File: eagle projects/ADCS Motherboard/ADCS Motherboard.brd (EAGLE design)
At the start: 91 x 91 mm, 127 parts, among them J1 HDR_10_EZFET_DEBUGGER, J3 HDR_2X5_GRPB052VWQS-RC, Q1 PMV16XN, Q2 IRLML6246TRPBF, Q3 IRLML2246TRPBF, U1 MSP430F5529IPN, U2 LMV321, U3 ADS7841E_2K5, U4 LMV321, U5 LMV321, U7 HMC1053, Y1 32.768kHz, Y2 CSTCR4M00G15L99, Y3 32.768kHz

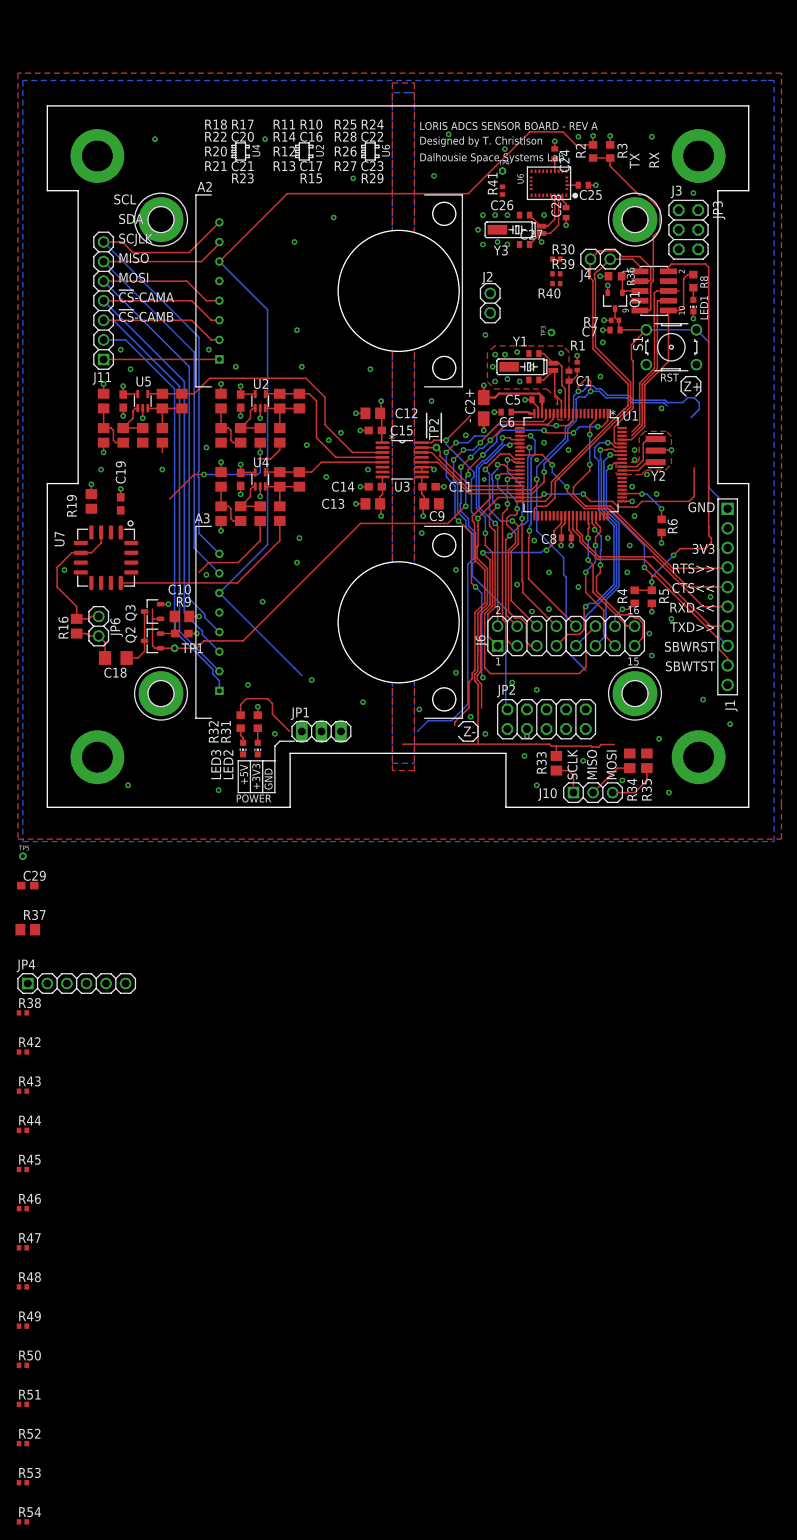
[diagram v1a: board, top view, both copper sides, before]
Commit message: Major layout changes check point
New connectors, analog plane reshape, moved msp430
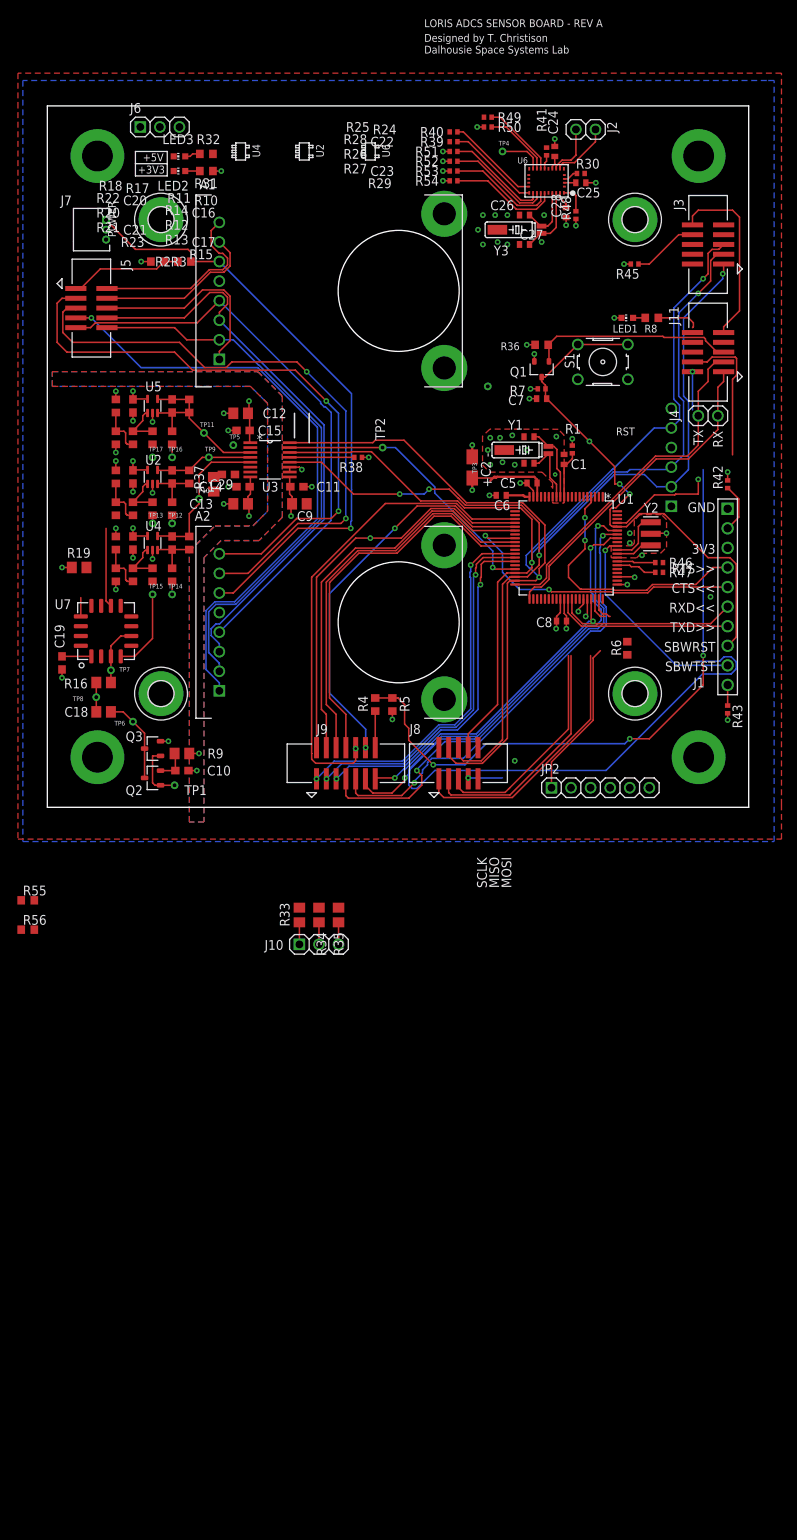
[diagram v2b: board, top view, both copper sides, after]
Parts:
- removed A3: ARDUCAM_OV5642, my_library:ARDUCAM
- removed JP1: (no value), pinhead:1X03
- removed JP3: (no value), pinhead:2X03
- removed JP6: (no value), my_library:1X02
- removed R44: 5.1M, rcl:R0402
- added A1: ARDUCAM_OV5642, my_library:ARDUCAM
- added J5, J8: CNC_3221-10-0300-00, my_library:CNC_3221-10-0300-00
- added J7: TE-1734829-3, my_library:TE-1734829-3
- added J9: CNC_3221-14-0300-00, my_library:CNC_3221-14-0300-00
- added R55, R56: 5.1M, rcl:R0603
- added TP10, TP11, TP12, TP13, TP14, TP15, TP16, TP17, TP6, TP7, TP8, TP9: TESTPOINT, my_library:TP_P76H50
- C17, C21, C23: device rcl:C0805 -> rcl:C0603
- C18: device resistor:C1206 -> rcl:C0805
- J11: value (none) -> CNC_3221-10-0300-00; device my_library:1X07 -> my_library:CNC_3221-10-0300-00
- J3: value HDR_2X5_GRPB052VWQS-RC -> CNC_3221-10-0300-00; device my_library:GRPB052VWQS-RC -> my_library:CNC_3221-10-0300-00
- J6: device my_library:2X08 -> my_library:1X03
- JP2: device pinhead:2X05 -> my_library:1X06
- R10, R11, R12, R13, R14, R15, R17, R18, R20, R21, R22, R23, R24, R25, R26, R27, R28, R29: device rcl:R0805 -> rcl:R0603
- R16: value 0R -> 1R
- moved R54 182.7 mm to (52.7, 81.3)
- moved R53 179.1 mm to (52.7, 82.5)
- moved R52 175.5 mm to (52.7, 83.8)
- moved R51 171.9 mm to (52.7, 85.1)
- moved R50 171.6 mm to (57.1, 88.3)
- moved R49 168.0 mm to (57.1, 89.5)
- moved R48 156.5 mm to (68.6, 76.8), turned to 90 degrees
- moved R45 141.8 mm to (76.2, 70.5), turned to 180 degrees
- moved R47 120.4 mm to (79.4, 30.5)
- moved R46 117.6 mm to (79.4, 31.8)
- moved R42 117.4 mm to (88.3, 41.9), turned to 90 degrees
- moved R43 104.0 mm to (88.3, 12.7), turned to 270 degrees
- moved JP4 103.0 mm to (81.0, 45.4), flipped to the bottom, turned to 90 degrees
- moved J6 84.5 mm to (14.6, 88.3)
- moved R38 84.2 mm to (40.3, 45.4), turned to 180 degrees
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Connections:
- removed net !CS!_CAM_A: A2.1, J11.1
- removed net !CS!_CAM_B: A3.1, J11.2
- removed net N$18: JP2.8, R45.1
- removed net N$19: JP2.10, R44.1
- removed net PAYLOAD_MISO: A2.3, A3.3, J11.4
- removed net PAYLOAD_MOSI: A2.2, A3.2, J11.3
- removed net PAYLOAD_SCL: A2.8, A3.8, J11.7
- removed net PAYLOAD_SCLK: A2.4, A3.4, J11.5
- removed net PAYLOAD_SDA: A2.7, A3.7, J11.6
- removed net SEN_BRD_5V_PRESENT: J3.9, R2.1, R3.2
- new net CAMERA-1_CS: A1.1, J5.6
- new net CAMERA-1_SCL: A1.8, J5.2
- new net CAMERA-1_SDA: A1.7, J5.4
- new net CAMERA-2_CS: A2.1, J5.7
- new net CAMERA-2_SCL: A2.8, J5.3
- new net CAMERA-2_SDA: A2.7, J5.5
- new net CAMERA_MISO: A1.3, A2.3, J5.8
- new net CAMERA_MOSI: A1.2, A2.2, J5.10
- new net CAMERA_SCLK: A1.4, A2.4, J5.9
- new net CAM_5V_PRESENT: J5.1, R2.1, R3.2
- new net N$55: J8.9, R56.2
- new net N$57: J8.10, R55.1
- new net N$58: J3.8, R45.1
- new net P1.0: JP2.6, U1.21
- new net P1.1: JP2.5, U1.22
- new net TB0.3: JP2.2, U1.58
- new net TB0.4: JP2.1, U1.59
- new net TB0.5: JP2.4, U1.42
- new net TB0.6: JP2.3, U1.43
- new net Z-_SUN_3V_PRESENT: J11.9, J3.10
- net !CS!_CURRENT_SENSE_1: now also J8.3; no longer JP3.1
- net !CS!_CURRENT_SENSE_2: now also J8.5; no longer JP3.3
- net !CS!_SUN_X+: now also J3.2; no longer JP2.2
- net !CS!_SUN_X-: now also J3.7; no longer JP2.7
- net !CS!_SUN_Y+: now also J3.4; no longer JP2.4
- net !CS!_SUN_Y-: now also J3.9; no longer JP2.9
- net !CS!_SUN_Z+: now also JP4.4; no longer JP4.5
- net !CS!_SUN_Z-: now also J3.6; no longer JP2.6
- net +3V3: now also J11.7, J6.2, J7.2; no longer J3.7, JP1.2
- net +5V: now also A1.6, J6.1, J7.1; no longer A3.6, JP1.1
- net ACT_BRD_3V_PRESENT: now also J11.4, J8.7; no longer J3.4, JP3.5
- net ACT_BRD_5V_PRESENT: now also J9.14; no longer J6.14
- net ACT_BRD_5V_SHIFTED: now also J11.2; no longer J3.2
- net B_MEAS_X: now also TP10.1
- net B_MEAS_Y: now also TP9.1
- net B_MEAS_Z: now also TP11.1
- net GND: now also A1.5, A1.P$1, A1.P$2, A2.P$1, A2.P$2, J6.3, J7.3, R55.2, R56.1; no longer A3.5, JP1.3, R44.2
- net MAG_X_FIN: now also J9.10; no longer J6.10
- net MAG_X_RIN: now also J9.12; no longer J6.12
- net MAG_Y_FIN: now also J9.6; no longer J6.6
- net MAG_Y_RIN: now also J9.8; no longer J6.8
- net MAG_Z_FIN: now also J9.2; no longer J6.2
- net MAG_Z_RIN: now also J9.4; no longer J6.4
- net MSP430_ACTIVE: now also J11.10; no longer J3.10
- net MSP_OBC_RESET: now also J11.5; no longer J3.5
- net N$35: now also TP8.1; no longer JP6.2
- net N$37: now also TP7.1; no longer JP6.1
- net N$9: now also TP6.1
- net OUT_A_N: now also TP13.1
- net OUT_A_P: now also TP12.1
- net OUT_B_N: now also TP15.1
- net OUT_B_P: now also TP14.1
- net OUT_C_N: now also TP17.1
- net OUT_C_P: now also TP16.1
- net RESERVED_1: now also J11.6; no longer J3.6
- net RESERVED_2: now also J11.8; no longer J3.8
- net RW_X_DIR: now also J9.7; no longer J6.7
- net RW_X_OUTFG: now also J9.13; no longer J6.13
- net RW_X_SPEED_CTRL: now also J9.1; no longer J6.1
- net RW_Y_DIR: now also J9.9; no longer J6.9
- net RW_Y_OUTFG: now also J8.1; no longer J6.15
- net RW_Y_SPEED_CTRL: now also J9.3; no longer J6.3
- net RW_Z_DIR: now also J9.11; no longer J6.11
- net RW_Z_OUTFG: now also J8.2; no longer J6.16
- net RW_Z_SPEED_CTRL: now also J9.5; no longer J6.5
- net UCA0RXD: now also J11.1; no longer J3.1
- net UCA0TXD: now also J11.3; no longer J3.3
- net UCB0_SPI_CLK: now also J3.5, J8.4, JP4.5; no longer JP2.5, JP3.2, JP4.4
- net UCB0_SPI_MISO: now also J3.1, J8.6; no longer JP2.1, JP3.4
- net UCB0_SPI_MOSI: now also J3.3, J8.8; no longer JP2.3, JP3.6
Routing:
- net RW_Z_DIR: track 28.8 -> 124.0 mm, vias 1 -> 2
- net CAMERA-2_CS: track 0.00 -> 79.6 mm, vias 0 -> 1
- net CAMERA-2_SCL: track 0.00 -> 78.6 mm, vias 0 -> 2
- net CAMERA-2_SDA: track 0.00 -> 78.5 mm, vias 0 -> 2
- net CAMERA_MISO: track 0.00 -> 76.1 mm
- net CAMERA_SCLK: track 0.00 -> 75.2 mm
- net HMC1053_RESET: track 81.5 -> 7.52 mm, vias 6 -> 0
- net CAMERA_MOSI: track 0.00 -> 72.9 mm
- net PAYLOAD_MOSI: track 68.6 -> 0.00 mm
- net PAYLOAD_MISO: track 67.8 -> 0.00 mm
- net PAYLOAD_SCLK: track 67.8 -> 0.00 mm
- net PAYLOAD_SCL: track 64.0 -> 0.00 mm
- net PAYLOAD_SDA: track 62.9 -> 0.00 mm
- net !CS!_SUN_Z-: track 55.9 -> 0.00 mm, vias 3 -> 0
- net !CS!_CAM_B: track 53.4 -> 0.00 mm
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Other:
- outline, holes or cut-outs redrawn
- board text removed: "!CS!-CAMA"
- board text removed: "!CS!-CAMB"
- board text removed: "J3"
- board text removed: "SCJLK"
- board text removed: "SCL"
- board text removed: "SDA"
- board text removed: "Z+"
- board text removed: "Z-"

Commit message: Draft of Rev B done
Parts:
- added TP18, TP19: TESTPOINT, my_library:TP_P76H50
- moved J10 112.0 mm to (74.9, 87.0), turned to 180 degrees
- moved R33 107.0 mm to (77.5, 83.2), turned to 90 degrees
- moved R34 104.9 mm to (74.9, 83.2), turned to 90 degrees
- moved R35 103.1 mm to (72.4, 83.2), turned to 90 degrees
- moved R56 71.2 mm to (63.2, 11.4), turned to 270 degrees
- moved R55 67.7 mm to (61.0, 11.4), turned to 90 degrees
- moved R4 39.7 mm to (82.2, 13.3)
- moved R5 39.7 mm to (84.5, 13.3)
- moved R40 24.8 mm to (60.6, 64.1), turned to 270 degrees
- moved R39 24.1 mm to (61.9, 64.1), turned to 270 degrees
- moved R51 23.6 mm to (63.5, 64.1), turned to 90 degrees
- moved R52 23.1 mm to (64.8, 64.1), turned to 90 degrees
- moved R53 22.7 mm to (66.0, 64.1), turned to 90 degrees
- moved R54 22.5 mm to (67.3, 64.1), turned to 90 degrees
- moved R50 19.4 mm to (57.1, 68.9)
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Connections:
- net P1.0: now also JP2.1; no longer JP2.6
- net P1.1: now also JP2.2; no longer JP2.5
- net TB0.3: now also JP2.5; no longer JP2.2
- net TB0.4: now also JP2.6; no longer JP2.1
- net TB0.5: now also JP2.3; no longer JP2.4
- net TB0.6: now also JP2.4; no longer JP2.3
- net UCB1_I2C_SCL: now also TP18.1
- net UCB1_I2C_SDA: now also TP19.1
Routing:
- net HMC1053_RESET: track 7.52 -> 98.8 mm, vias 0 -> 1
- net !CS!_SUN_X+: track 0.00 -> 79.2 mm, vias 0 -> 2
- net RW_Z_DIR: track 124.0 -> 58.0 mm
- net ACT_BRD_3V_PRESENT: track 23.3 -> 82.6 mm, vias 1 -> 4
- net RESERVED_2: track 0.00 -> 57.9 mm, vias 0 -> 2
- net !CS!_SUN_X-: track 0.07 -> 57.5 mm, vias 0 -> 2
- net RESERVED_1: track 0.00 -> 53.6 mm, vias 0 -> 2
- net !CS!_SUN_Y-: track 0.00 -> 52.4 mm, vias 0 -> 2
- net BNO055_RST: track 1.85 -> 53.2 mm, vias 0 -> 2
- net UCB1_I2C_SCL: track 12.2 -> 61.8 mm, vias 0 -> 2
- net !CS!_SUN_Z-: track 0.00 -> 48.5 mm, vias 0 -> 2
- net UCB1_I2C_SDA: track 12.1 -> 59.6 mm, vias 0 -> 2
- net P1.0: track 0.00 -> 40.8 mm, vias 0 -> 3
- net ACT_BRD_5V_SHIFTED: track 85.7 -> 45.7 mm, vias 4 -> 2
- net BNO055_INT: track 5.75 -> 45.5 mm, vias 0 -> 1
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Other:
- board text added: "ADCS MOTHER BOARD REV B"
- board text added: "Designer: Thomas Christison"
- board text added: "U5"
- board text removed: "Dalhousie Space Systems Lab"
- board text removed: "Designed by T. Christison"
- board text removed: "LORIS ADCS SENSOR BOARD - REV A"
- board text removed: "U6"

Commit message: More board layout updates
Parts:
- moved LED2 81.9 mm to (28.6, 3.17), turned to 180 degrees
- moved R31 79.5 mm to (28.6, 6.03), turned to 270 degrees
- moved LED3 79.5 mm to (26.4, 3.17), turned to 180 degrees
- moved R32 77.0 mm to (26.4, 6.03), turned to 270 degrees
- moved S1 48.6 mm to (71.4, 7.62), turned to 180 degrees
- moved Q1 8.91 mm to (74.3, 56.2)
- moved R36 8.91 mm to (74.3, 59.4)
- moved R7 8.91 mm to (74.3, 53.7)
- moved C7 8.90 mm to (74.3, 52.1)
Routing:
- net RST/SBWTDIO: track 61.8 -> 80.7 mm
- net +5V: track 97.5 -> 116.0 mm
- net !CS!_SUN_X+: track 79.2 -> 69.8 mm, vias 2 -> 3
- net MSP_OBC_RESET: track 26.0 -> 16.9 mm
- net +3V3: track 66.4 -> 62.6 mm, vias 20 -> 21
- net MAG_Z_FIN: track 52.0 -> 52.9 mm
- net CAMERA_SCLK: track 76.3 -> 75.5 mm
- net RESERVED_2: track 57.9 -> 57.4 mm
- net GND: track 63.1 -> 62.7 mm, vias 67 -> 102
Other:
- board text added: "+X"
- board text added: "+Y"

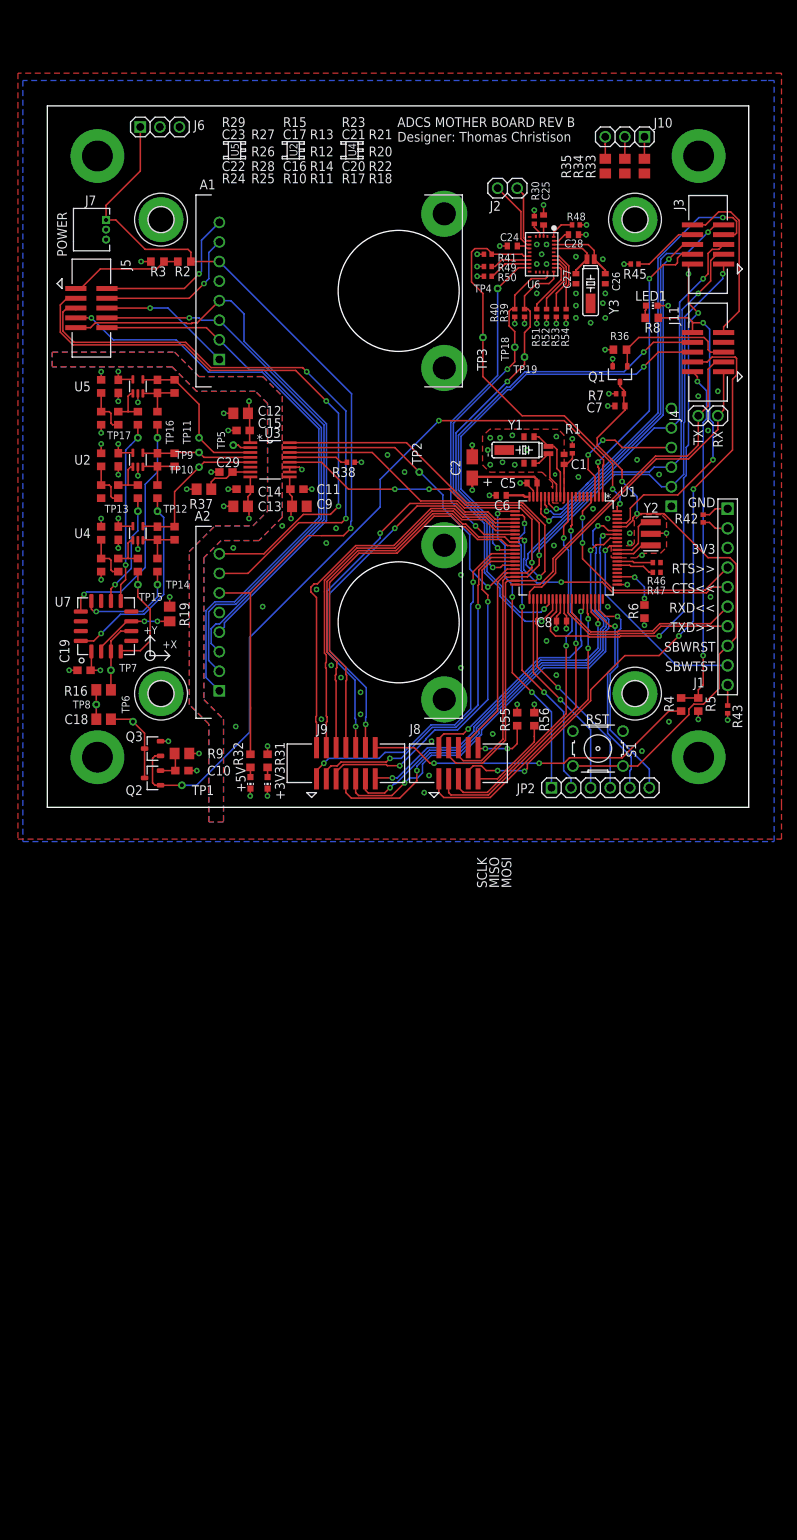
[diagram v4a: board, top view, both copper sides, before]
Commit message: Updated motherboad layout
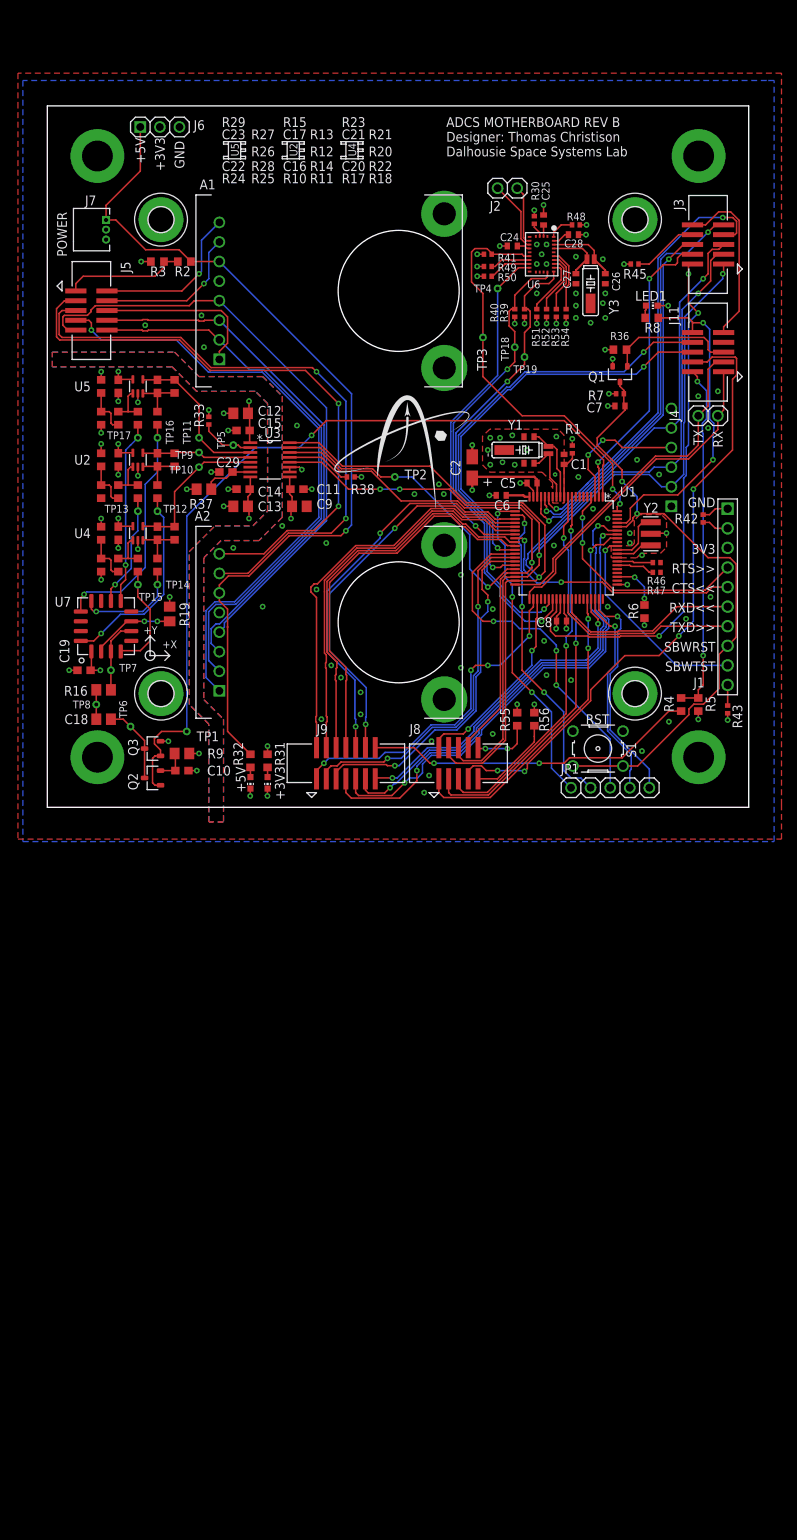
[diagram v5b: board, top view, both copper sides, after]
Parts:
- removed J10: (no value), my_library:1X03
- removed JP2: (no value), my_library:1X06
- removed R34, R35: 0R, rcl:R0805
- added JP1: (no value), my_library:1X05
- R33: value 0R -> 5.1M; device rcl:R0805 -> rcl:R0402
- moved R33 65.5 mm to (21.0, 50.2), turned to 270 degrees
- moved TP1 7.01 mm to (18.1, 9.84)
- moved TP2 3.24 mm to (45.1, 42.9), turned to 270 degrees
- moved R38 1.91 mm to (39.4, 42.9)
- moved TP6 0.71 mm to (10.8, 10.5)
- moved J5 0.32 mm to (5.71, 64.5)
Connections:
- removed net N$1: J10.1, R33.2
- removed net N$2: J10.2, R34.2
- removed net N$3: J10.3, R35.2
- removed net TB0.5: JP2.3, U1.42
- removed net TB0.6: JP2.4, U1.43
- new net P2.3: JP1.3, U1.32
- net GND: now also R33.1
- net N$29: now also R33.2
- net P1.0: now also JP1.1; no longer JP2.1
- net P1.1: now also JP1.2; no longer JP2.2
- net RW_X_SPEED_CTRL: now also U1.42; no longer U1.32
- net RW_Z_OUTFG: now also U1.43; no longer U1.55
- net TB0.3: now also JP1.4; no longer JP2.5
- net TB0.4: now also JP1.5; no longer JP2.6
- net UCB0_SPI_CLK: no longer R33.1
- net UCB0_SPI_MISO: no longer R34.1
- net UCB0_SPI_MOSI: no longer R35.1
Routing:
- net P2.3: track 0.00 -> 45.6 mm, vias 0 -> 3
- net TB0.6: track 28.5 -> 0.00 mm, vias 1 -> 0
- net TB0.5: track 27.6 -> 0.00 mm, vias 1 -> 0
- net HMC1053_RESET: track 98.8 -> 106.8 mm
- net RW_Z_OUTFG: track 30.9 -> 26.1 mm
- net N$29: track 2.34 -> 7.14 mm
- net RW_X_SPEED_CTRL: track 48.7 -> 43.9 mm, vias 2 -> 4
- net CAMERA-1_CS: track 17.3 -> 22.1 mm, vias 1 -> 0
- net CAMERA_SCLK: track 75.5 -> 78.9 mm
- net CAMERA-2_SDA: track 77.8 -> 80.7 mm
- net N$3: track 2.86 -> 0.00 mm
- net N$2: track 2.86 -> 0.00 mm
- net N$1: track 2.86 -> 0.00 mm
- net P1.1: track 39.6 -> 41.4 mm
- net CAMERA-2_SCL: track 76.4 -> 78.1 mm
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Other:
- board text added: "ADCS MOTHERBOARD REV B"
- board text added: "Dalhousie Space Systems Lab"
- board text removed: "ADCS MOTHER BOARD REV B"
- board text removed: "MISO"
- board text removed: "MOSI"
- board text removed: "SCLK"

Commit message: Last commit before major layout changes on Actuator board Rev B
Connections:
- net !CS!_CURRENT_SENSE_1 renamed !CS!_CURR_SENSE_RW
- net !CS!_CURRENT_SENSE_2 renamed !CS!_CURR_SENSE_MTQR
